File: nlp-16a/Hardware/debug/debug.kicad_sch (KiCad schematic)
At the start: 12 parts, among them J1 Conn_01x04_Female, J2 Conn_01x04_Male, J3 Conn_01x02_Male, J4 Conn_02x20_Odd_Even, J5 Conn_02x10_Odd_Even, J6 Conn_02x10_Odd_Even, J7 Conn_02x10_Odd_Even, J8 Conn_02x10_Odd_Even, U1 CH32V003F4P6

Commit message: 基板修正
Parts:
- added R2: 4.7k, Resistor_SMD:R_0603_1608Metric_Pad0.98x0.95mm_HandSolder, symbol Device:R
- C1: footprint Capacitor_SMD:C_0201_0603Metric_Pad0.64x0.40mm_HandSolder -> Capacitor_SMD:C_0603_1608Metric_Pad1.08x0.95mm_HandSolder
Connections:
- net VDD: now also R2.2
- net at J2.3 (Pin_3), U1.3 (PD6/URX): now also R2.1
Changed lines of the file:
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@@
   (junction (at 68.58 179.07) (diameter 0) (color 0 0 0 0)
+  )
+  (junction (at 82.55 171.45) (diameter 0) (color 0 0 0 0)
   )
   (junction (at 63.5 179.07) (diameter 0) (color 0 0 0 0)
@@
     (stroke (width 0) (type default) (color 0 0 0 0))
   )
+  (wire (pts (xy 82.55 171.45) (xy 82.55 181.61))
+    (stroke (width 0) (type default) (color 0 0 0 0))
+  )
   (bus (pts (xy 144.78 69.85) (xy 144.78 72.39))
     (stroke (width 0) (type default) (color 0 0 0 0))
@@
     (stroke (width 0) (type default) (color 0 0 0 0))
   )
-  (wire (pts (xy 82.55 167.64) (xy 82.55 181.61))
+  (wire (pts (xy 82.55 167.64) (xy 82.55 171.45))
     (stroke (width 0) (type default) (color 0 0 0 0))
   )
@@
     (stroke (width 0) (type default) (color 0 0 0 0))
   )
+  (wire (pts (xy 82.55 171.45) (xy 87.63 171.45))
+    (stroke (width 0) (type default) (color 0 0 0 0))
+  )
   (wire (pts (xy 74.93 153.67) (xy 74.93 179.07))
     (stroke (width 0) (type default) (color 0 0 0 0))
@@
     (stroke (width 0) (type default) (color 0 0 0 0))
   )
+  (wire (pts (xy 95.25 171.45) (xy 97.79 171.45))
+    (stroke (width 0) (type default) (color 0 0 0 0))
+  )
   (wire (pts (xy 88.9 82.55) (xy 109.22 82.55))
     (stroke (width 0) (type default) (color 0 0 0 0))
@@
   )
   (wire (pts (xy 170.18 72.39) (xy 190.5 72.39))
+    (stroke (width 0) (type default) (color 0 0 0 0))
+  )
+  (wire (pts (xy 97.79 171.45) (xy 97.79 170.18))
     (stroke (width 0) (type default) (color 0 0 0 0))
   )
@@
       (effects (font (size 1.27 1.27)) (justify left))
     )
-    (property "Footprint" "Capacitor_SMD:C_0201_0603Metric_Pad0.64x0.40mm_HandSolder" (id 2) (at 69.5452 186.69 0)
+    (property "Footprint" "Capacitor_SMD:C_0603_1608Metric_Pad1.08x0.95mm_HandSolder" (id 2) (at 69.5452 186.69 0)
       (effects (font (size 1.27 1.27)) hide)
     )
     (property "Datasheet" "~" (id 3) (at 68.58 182.88 0)
+      (effects (font (size 1.27 1.27)) hide)
+    )
+    (pin "1")
+    (pin "2")
+  )
+  (symbol (lib_id "Device:R") (at 91.44 171.45 90) (unit 1)
+    (in_bom yes) (on_board yes) (fields_autoplaced)
+    (property "Reference" "R2" (id 0) (at 91.44 165.1 90))
+    (property "Value" "4.7k" (id 1) (at 91.44 167.64 90))
+    (property "Footprint" "Resistor_SMD:R_0603_1608Metric_Pad0.98x0.95mm_HandSolder" (id 2) (at 91.44 173.228 90)
+      (effects (font (size 1.27 1.27)) hide)
+    )
+    (property "Datasheet" "~" (id 3) (at 91.44 171.45 0)
       (effects (font (size 1.27 1.27)) hide)
     )
@@
     )
     (property "Datasheet" "" (id 3) (at 133.35 182.88 0)
+      (effects (font (size 1.27 1.27)) hide)
+    )
+    (pin "1")
+  )
+  (symbol (lib_id "power:VDD") (at 97.79 170.18 0) (unit 1)
+    (in_bom yes) (on_board yes)
+    (property "Reference" "#PWR06" (id 0) (at 97.79 173.99 0)
+      (effects (font (size 1.27 1.27)) hide)
+    )
+    (property "Value" "VDD" (id 1) (at 100.33 166.37 0))
+    (property "Footprint" "" (id 2) (at 97.79 170.18 0)
+      (effects (font (size 1.27 1.27)) hide)
+    )
+    (property "Datasheet" "" (id 3) (at 97.79 170.18 0)
       (effects (font (size 1.27 1.27)) hide)
     )
@@
       (reference "#PWR05") (unit 1) (value "GND") (footprint "")
     )
+    (path "/b760f969-5b95-4648-ab7c-956803c54444"
+      (reference "#PWR06") (unit 1) (value "VDD") (footprint "")
+    )
     (path "/43990c42-b07b-45f0-bdc8-1f3b67ad9710"
-      (reference "C1") (unit 1) (value "0.1u") (footprint "Capacitor_SMD:C_0201_0603Metric_Pad0.64x0.40mm_HandSolder")
+      (reference "C1") (unit 1) (value "0.1u") (footprint "Capacitor_SMD:C_0603_1608Metric_Pad1.08x0.95mm_HandSolder")
     )
     (path "/d4b0193e-ff47-4085-bd95-4d50ec331b94"
@@
       (reference "R1") (unit 1) (value "470") (footprint "Resistor_SMD:R_0603_1608Metric_Pad0.98x0.95mm_HandSolder")
     )
+    (path "/545f3b90-c40a-4879-977a-91c18a9b05e3"
+      (reference "R2") (unit 1) (value "4.7k") (footprint "Resistor_SMD:R_0603_1608Metric_Pad0.98x0.95mm_HandSolder")
+    )
     (path "/6ce67e8a-52e8-47c8-9498-19c4a3b55c74"

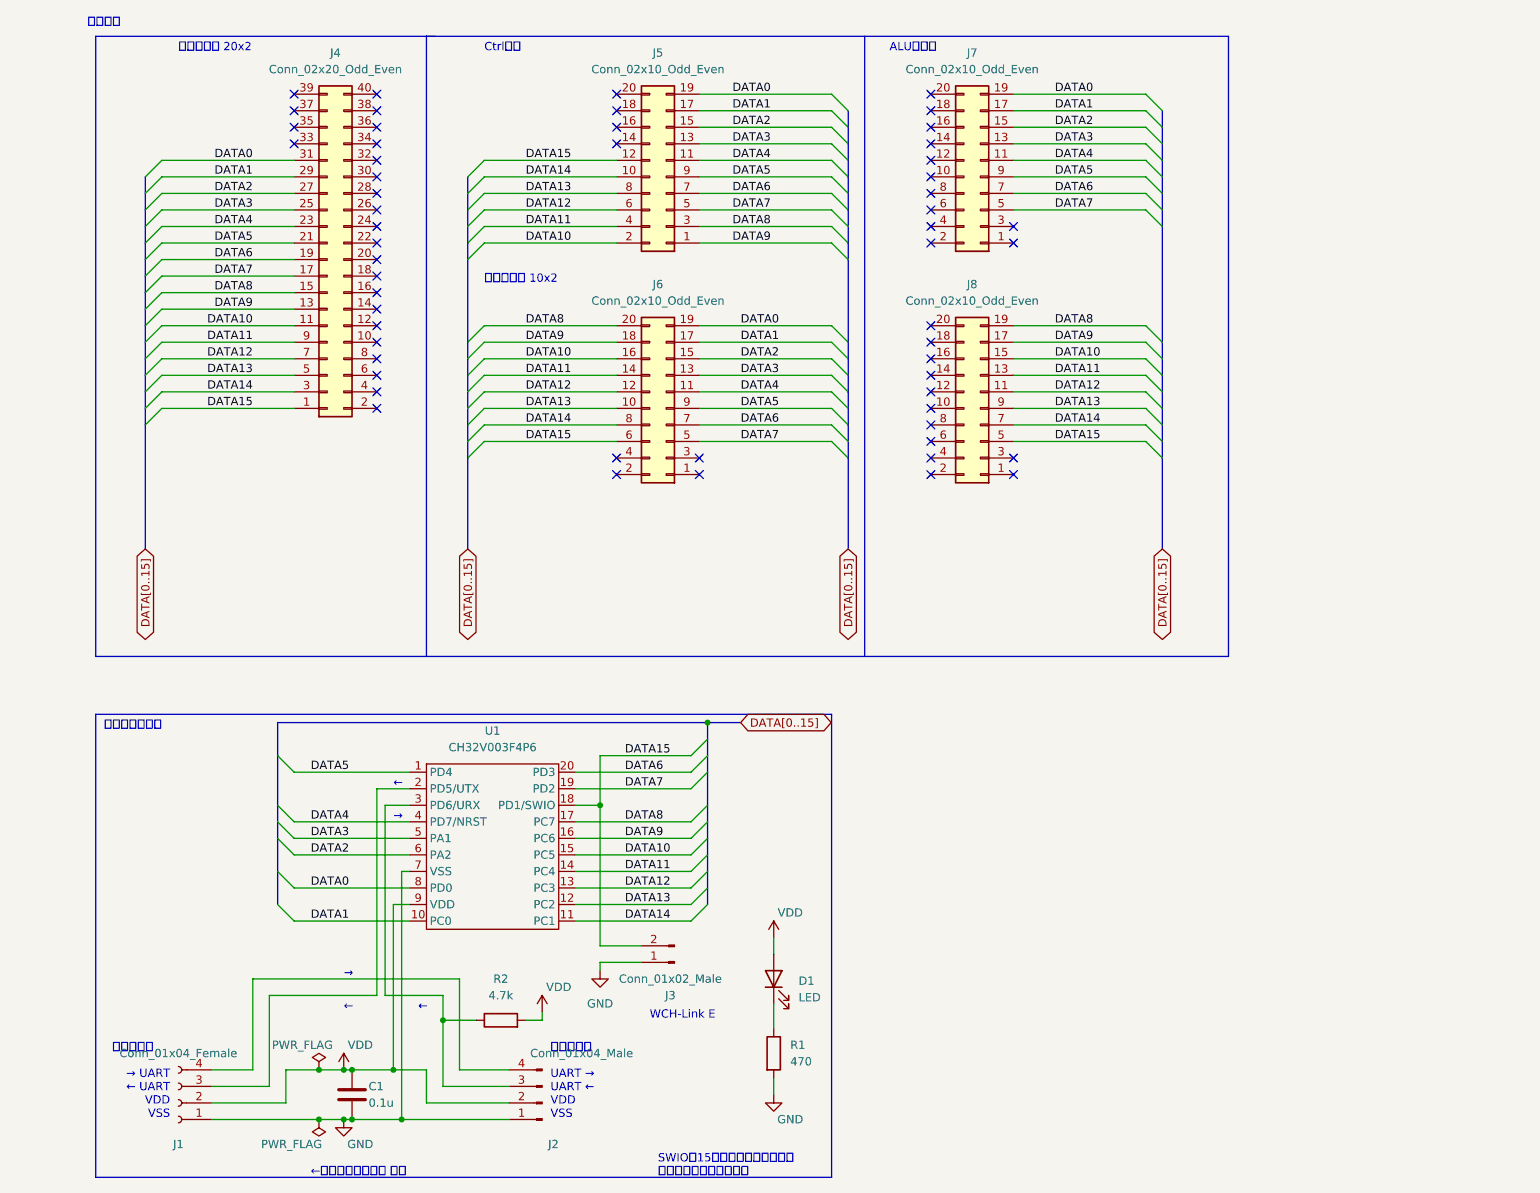
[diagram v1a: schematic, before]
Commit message: デバッガ基板の設計完了
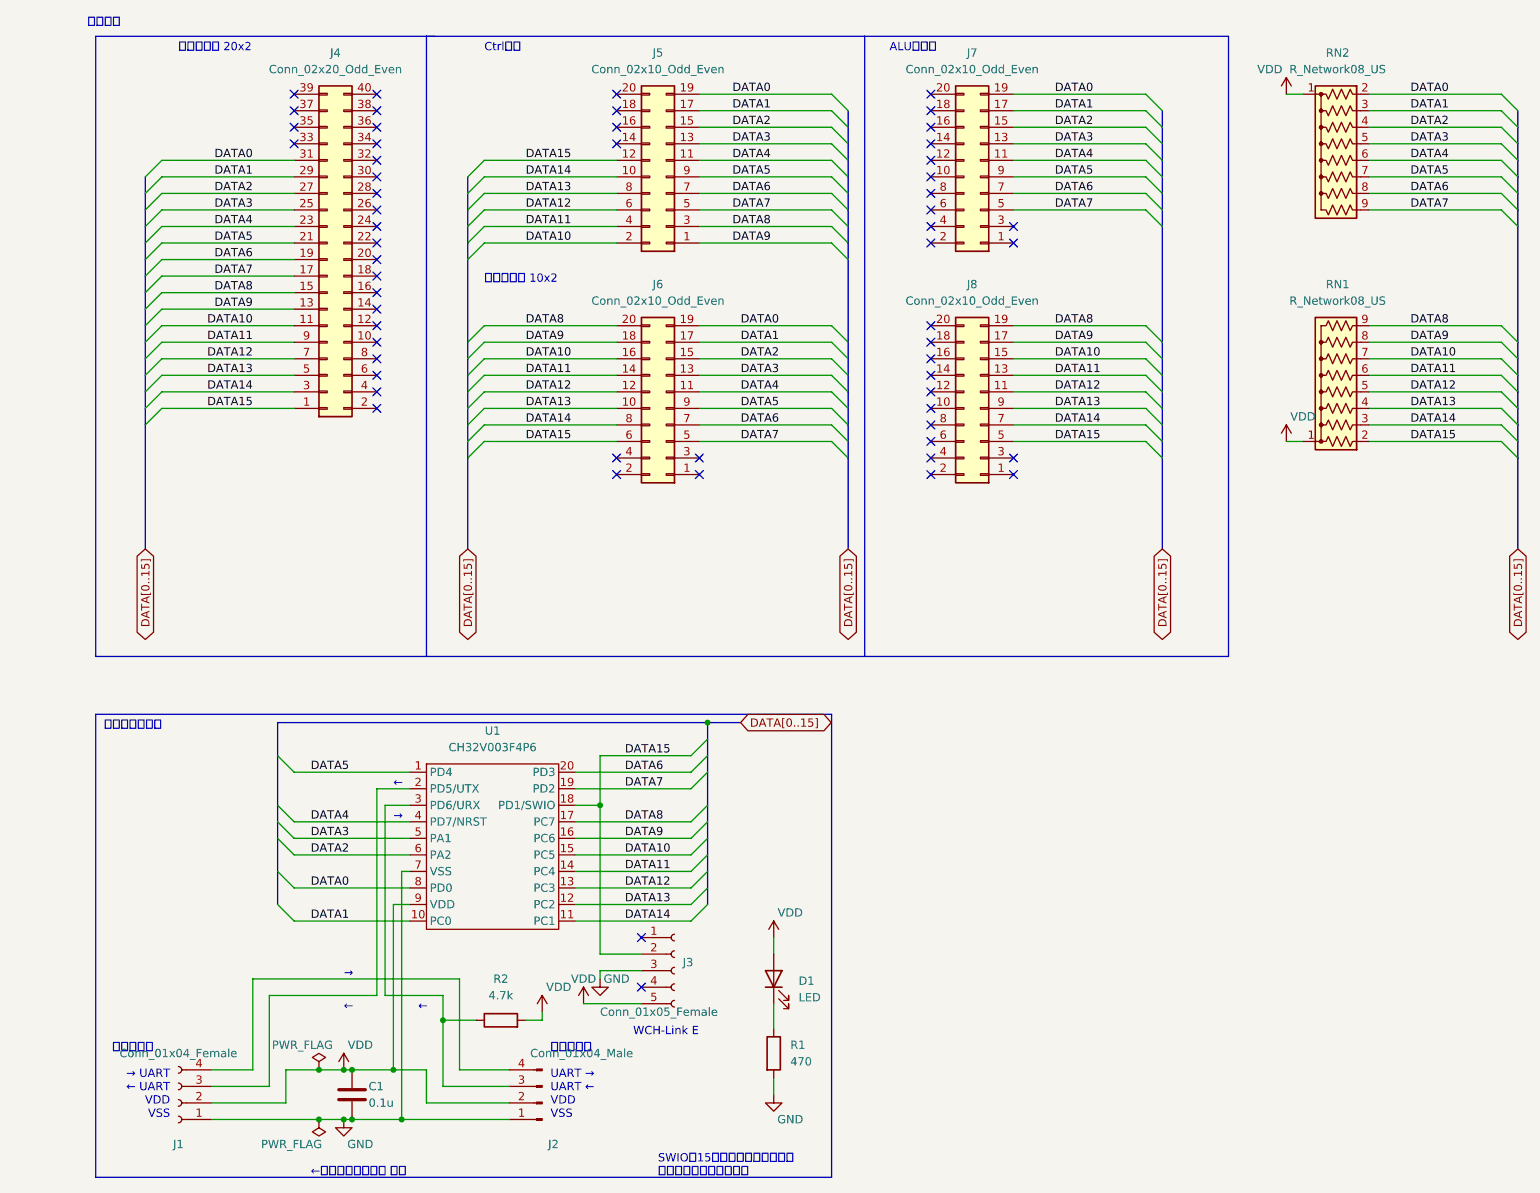
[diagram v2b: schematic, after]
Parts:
- removed J3: Conn_01x02_Male, Connector_PinSocket_2.54mm:PinSocket_1x02_P2.54mm_Vertical, symbol Connector:Conn_01x02_Male
- added J3: Conn_01x05_Female, Connector_PinSocket_2.54mm:PinSocket_1x05_P2.54mm_Horizontal, symbol Connector:Conn_01x05_Female
- added RN1, RN2: R_Network08_US, Resistor_THT:R_Array_SIP9, symbol Device:R_Network08_US
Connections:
- net DATA0: now also RN2.2 (R1)
- net DATA1: now also RN2.3 (R2)
- net DATA10: now also RN1.7 (R6)
- net DATA11: now also RN1.6 (R5)
- net DATA12: now also RN1.5 (R4)
- net DATA13: now also RN1.4 (R3)
- net DATA14: now also RN1.3 (R2)
- net DATA15: now also J3.2 (Pin_2), RN1.2 (R1)
- net DATA2: now also RN2.4 (R3)
- net DATA3: now also RN2.5 (R4)
- net DATA4: now also RN2.6 (R5)
- net DATA5: now also RN2.7 (R6)
- net DATA6: now also RN2.8 (R7)
- net DATA7: now also RN2.9 (R8)
- net DATA8: now also RN1.9 (R8)
- net DATA9: now also RN1.8 (R7)
- net GND: now also J3.3 (Pin_3)
- net VDD: now also J3.5 (Pin_5), RN1.1 (common), RN2.1 (common)
- no-connect marks 56 -> 58

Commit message: デバッガ基板の設計今度こそ完了
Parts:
- removed J1: Conn_01x04_Female, Connector_PinSocket_2.54mm:PinSocket_1x04_P2.54mm_Horizontal, symbol Connector:Conn_01x04_Female
- removed J2: Conn_01x04_Male, Connector_PinHeader_2.54mm:PinHeader_1x04_P2.54mm_Horizontal, symbol Connector:Conn_01x04_Male
- removed J3: Conn_01x05_Female, Connector_PinSocket_2.54mm:PinSocket_1x05_P2.54mm_Horizontal, symbol Connector:Conn_01x05_Female
- added J1: Conn_01x06_Male, Connector_PinHeader_2.54mm:PinHeader_1x06_P2.54mm_Horizontal, symbol Connector:Conn_01x06_Male
- added J2, J3: Conn_01x06_Female, Connector_PinSocket_2.54mm:PinSocket_1x06_P2.54mm_Horizontal, symbol Connector:Conn_01x06_Female
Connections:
- net DATA15: now also J3.3 (Pin_3)
- net GND: now also J1.1 (Pin_1), J2.1 (Pin_1), J3.4 (Pin_4)
- net VDD: now also J1.2 (Pin_2), J2.2 (Pin_2), J3.6 (Pin_6)
- net at R2.1, U1.3 (PD6/URX): now also J1.3 (Pin_3)
- net at U1.2 (PD5/UTX): now also J2.3 (Pin_3)
- new net: J1.4 (Pin_4), J2.4 (Pin_4)
- no-connect marks 58 -> 63

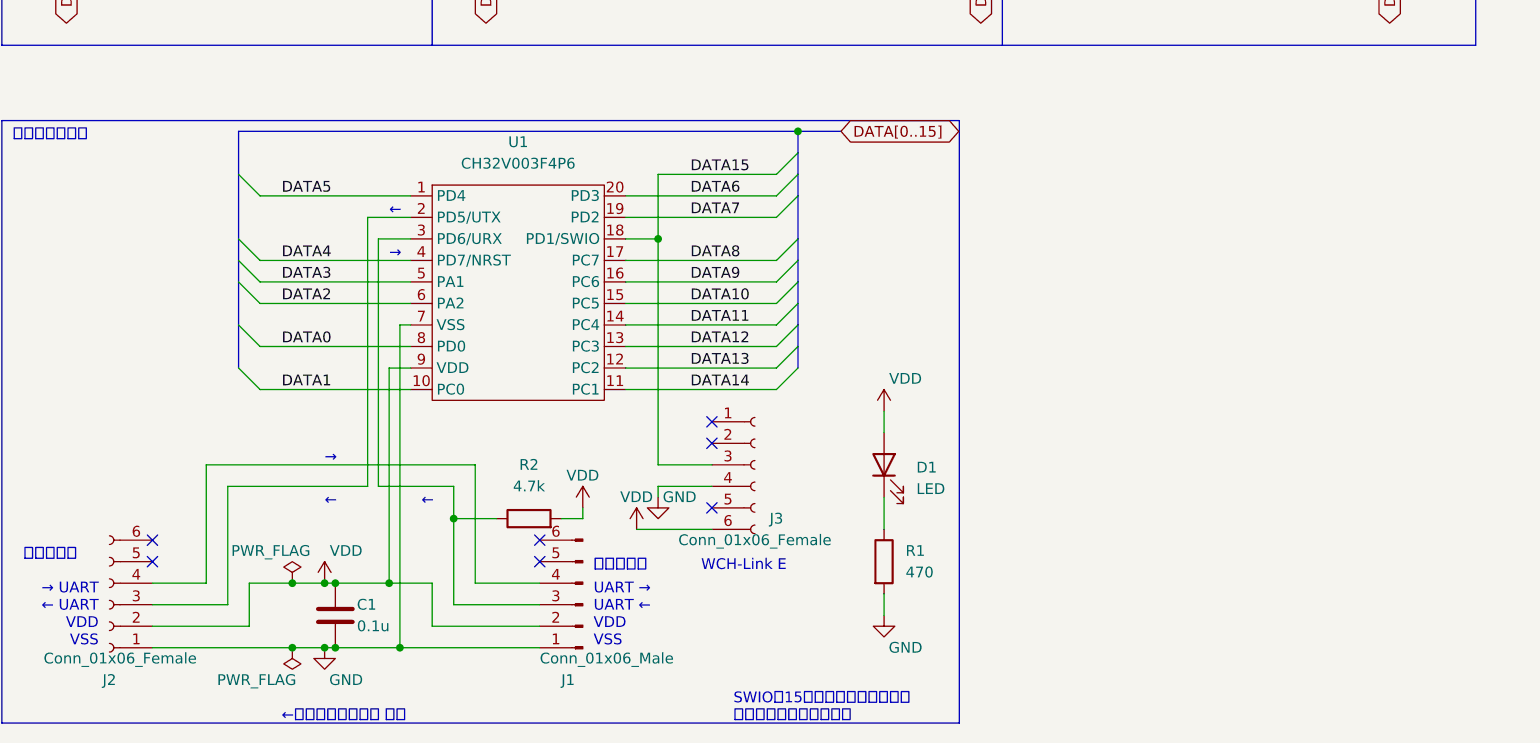
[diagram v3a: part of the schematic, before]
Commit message: v1.1全ガーバーを更新
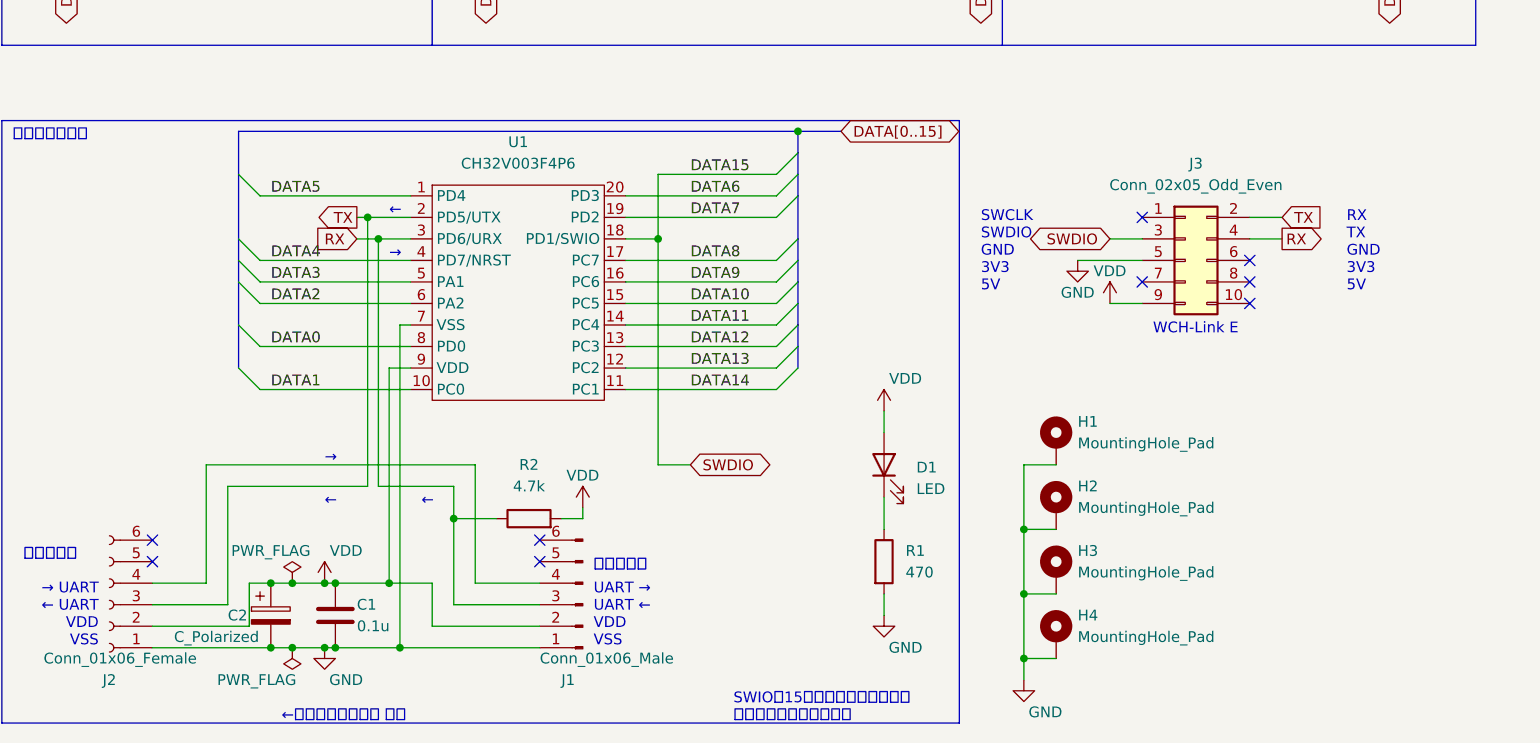
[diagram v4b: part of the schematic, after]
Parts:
- removed J3: Conn_01x06_Female, Connector_PinSocket_2.54mm:PinSocket_1x06_P2.54mm_Horizontal, symbol Connector:Conn_01x06_Female
- added C2: C_Polarized, Capacitor_THT:CP_Radial_D5.0mm_P2.50mm, symbol Device:C_Polarized
- added H1, H2, H3, H4: MountingHole_Pad, MountingHole:MountingHole_3.2mm_M3_Pad, symbol Mechanical:MountingHole_Pad
- added J3: Conn_02x05_Odd_Even, Connector_PinHeader_2.54mm:PinHeader_2x05_P2.54mm_Vertical, symbol Connector_Generic:Conn_02x05_Odd_Even
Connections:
- net GND: now also C2.2, H1.1, H2.1, H3.1, H4.1, J3.5 (Pin_5)
- net VDD: now also C2.1, J3.9 (Pin_9)
- net RX: now reaches J1.3 (Pin_3), R2.1, U1.3 (PD6/URX)
- net RX: now also J3.4 (Pin_4)
- net TX: now reaches J2.3 (Pin_3), U1.2 (PD5/UTX)
- net TX: now also J3.2 (Pin_2)
- net DATA15 renamed SWDIO
- net SWDIO: now also J3.3 (Pin_3)
- no-connect marks 63 -> 65
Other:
- note added: "RX TX GND 3V3 5V"
- note added: "SWCLK SWDIO GND 3V3 5V"

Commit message: デバッガ改良
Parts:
- added J9: Conn_01x02_Male, Connector_PinHeader_2.54mm:PinHeader_1x02_P2.54mm_Vertical, symbol Connector:Conn_01x02_Male
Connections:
- net RX: now also J1.4 (Pin_4); no longer J1.3 (Pin_3)
- net TX: now also J2.4 (Pin_4), J9.2 (Pin_2); no longer J2.3 (Pin_3)
- net VDD: now also J1.3 (Pin_3), J2.3 (Pin_3); no longer J1.2 (Pin_2), J2.2 (Pin_2)
- net at J1.5 (Pin_5): now also J2.5 (Pin_5), J9.1 (Pin_1)
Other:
- note added: "RTS TX→ ←RX VCC CTS GND"
- note added: "RTS →RX ←TX VCC CTS GND"
